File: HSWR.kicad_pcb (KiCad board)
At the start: 4 copper layers, 152 x 139 mm, 158 parts, among them IC1 B1212S-2W, IC2 JW5052C, IC3 JW5052C, IC4 ADUM3054, IC5 ADuM4160, J1 USB_B, J2 IO, J3 B+, J4 B-, J5 U, J6 V, J7 W, J8 SWD, J9 AVR-ISP-6, Q1 IXFK300N20X3, Q2 IXFK300N20X3, Q3 IXFK300N20X3, Q4 IXFK300N20X3, Q5 IXFK300N20X3, Q6 IXFK300N20X3, Q7 Q_NMOS_GSD, U1 ACS781xLRTR-150B, U10 AM26LV32xD, U11 ADuM120N, U12 ADuM120N, U13 PC355, U2 ACS781xLRTR-150B, U3 ACS781xLRTR-150B, U4 STM32F405RGTx, U5 IRS2186, U6 IRS2186, U7 IRS2186, U8 AP1117-50, U9 ATtiny13A-SU, Y1 8MHz

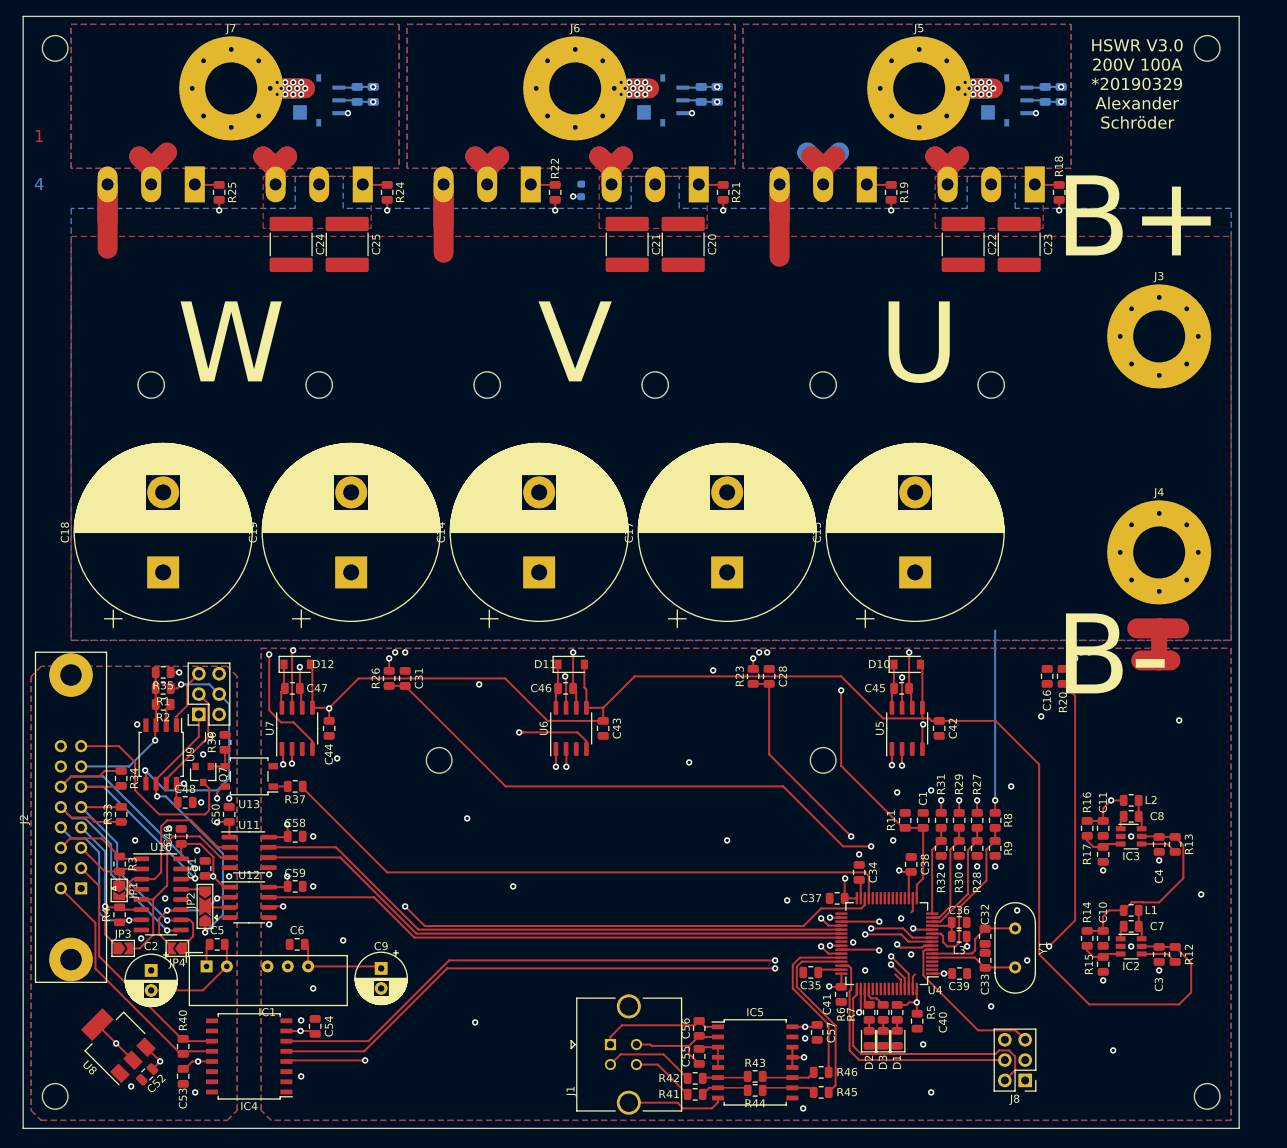
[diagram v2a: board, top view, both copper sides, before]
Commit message: - optimized silk screen - fixed some final missing traces
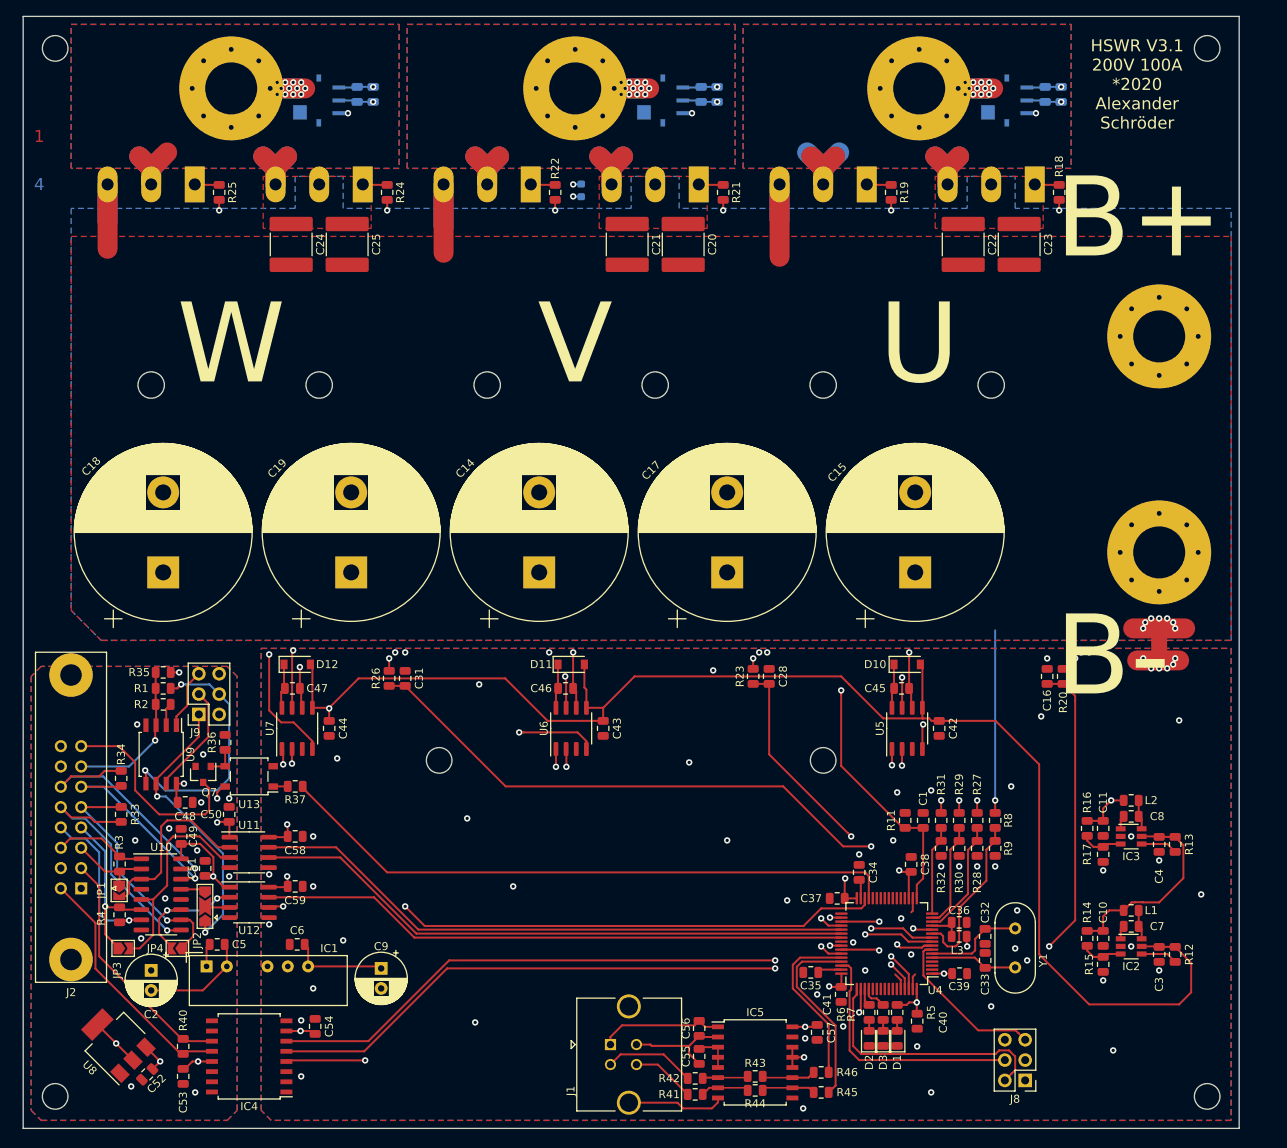
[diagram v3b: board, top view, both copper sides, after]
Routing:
- net +3V3: track 282.3 -> 343.1 mm, vias 18 -> 20
- net /MCU/U_I: track 58.9 -> 60.9 mm
- net GND: track 240.3 -> 241.9 mm, vias 54 -> 65
- net GNDPWR: track 45.4 -> 46.6 mm, vias 0 -> 7
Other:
- board text added: "HSWR V3.1 200V 100A *2020 Alexander Schröder"
- board text removed: "HSWR V3.0 200V 100A *20190329 Alexander Schröder"

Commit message: - fixed ISP connector being mirrored - changed some footprints to get them 3D Models - added a preliminary BOM
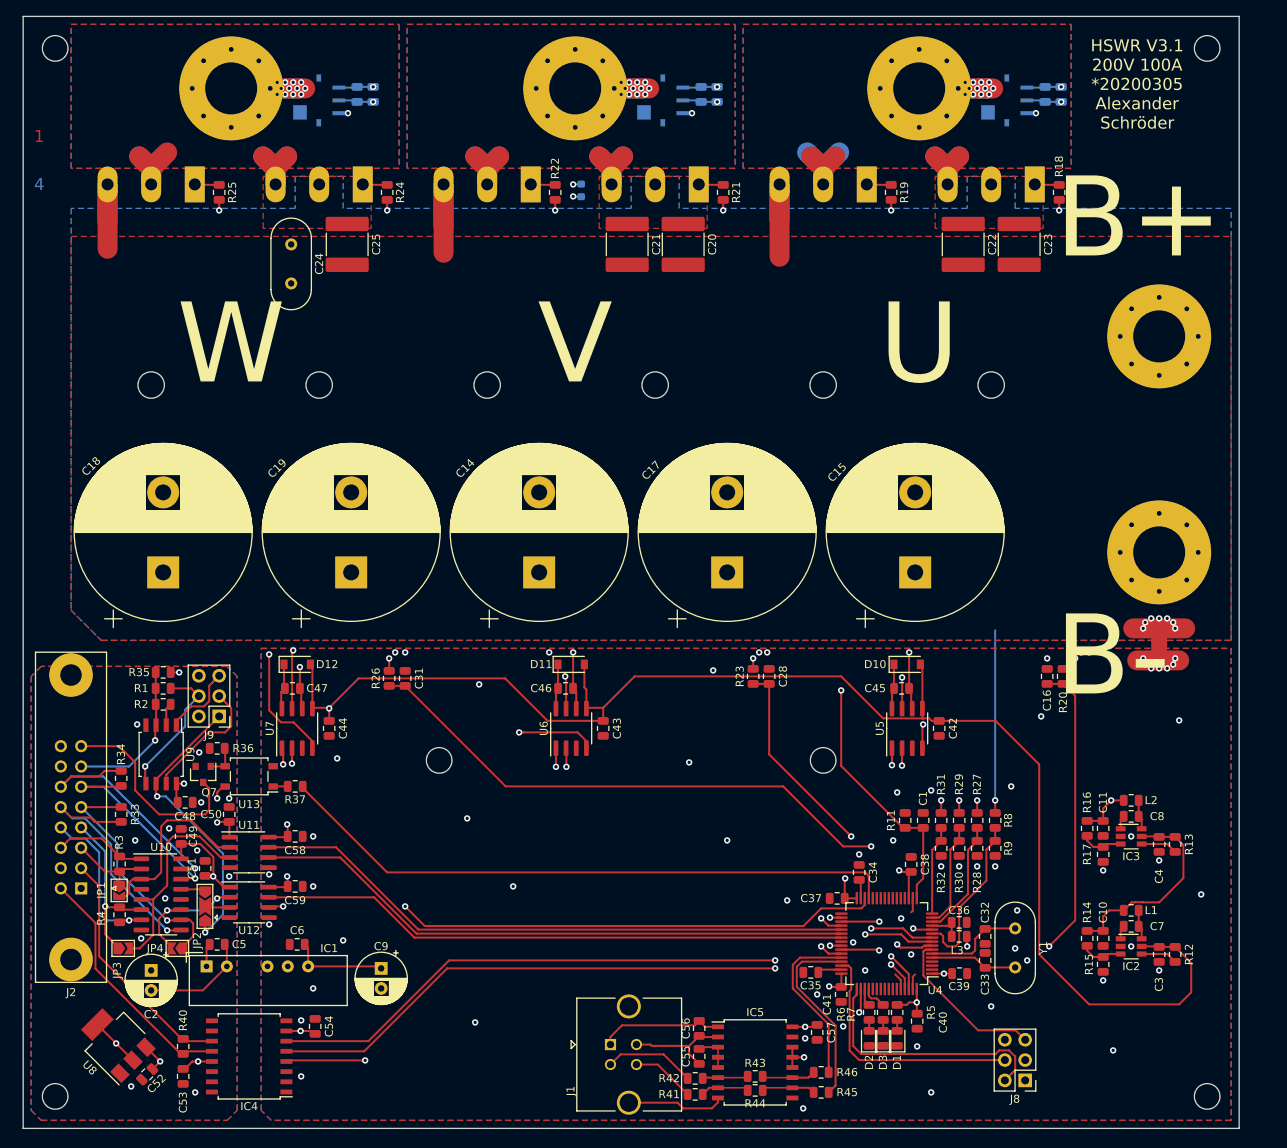
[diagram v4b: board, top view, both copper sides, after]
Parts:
- C24: footprint Capacitor_SMD:C_2220_5650Metric -> Crystal:Crystal_HC49-4H_Vertical
- J9: footprint Connector_PinSocket_2.54mm:PinSocket_2x03_P2.54mm_Vertical -> Connector_PinHeader_2.54mm:PinHeader_2x03_P2.54mm_Vertical
- U5, U6, U7: footprint Package_SO:SO-8_3.9x4.9mm_P1.27mm -> Package_SO:SOIC-8_3.9x4.9mm_P1.27mm
- Y1: footprint Crystal:Crystal_HC49-U_Vertical -> Crystal:Crystal_HC49-4H_Vertical
- moved J9 2.55 mm to (91.5, 111.5)
- moved R36 1.25 mm to (91.2, 115.5), turned to 180 degrees
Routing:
- net Net-(J9-Pad4): track 31.7 -> 17.7 mm, vias 2 -> 1
- net Net-(J9-Pad3): track 13.9 -> 16.1 mm
- net Net-(J9-Pad5): track 7.59 -> 9.33 mm
- net Net-(J9-Pad1): track 35.7 -> 36.5 mm
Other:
- board text added: "HSWR V3.1 200V 100A *20200305 Alexander Schröder"
- board text removed: "HSWR V3.1 200V 100A *2020 Alexander Schröder"

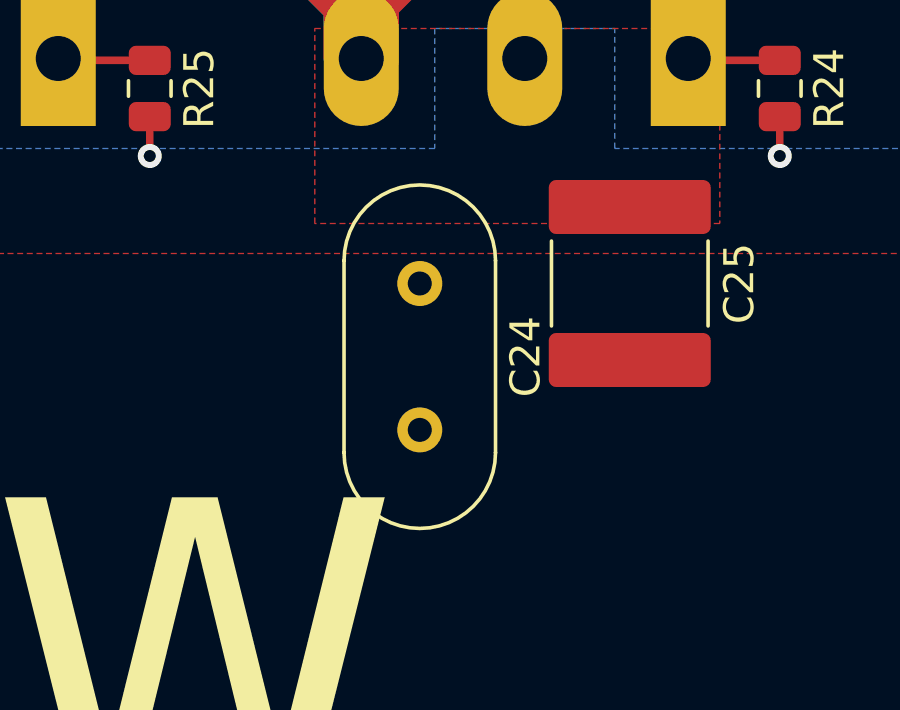
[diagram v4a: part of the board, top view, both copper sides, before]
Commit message: - removed some unused symbols from HSWR.lib - changed U8 (linear reg) to standard symbol - fixed wrong footprint for C24
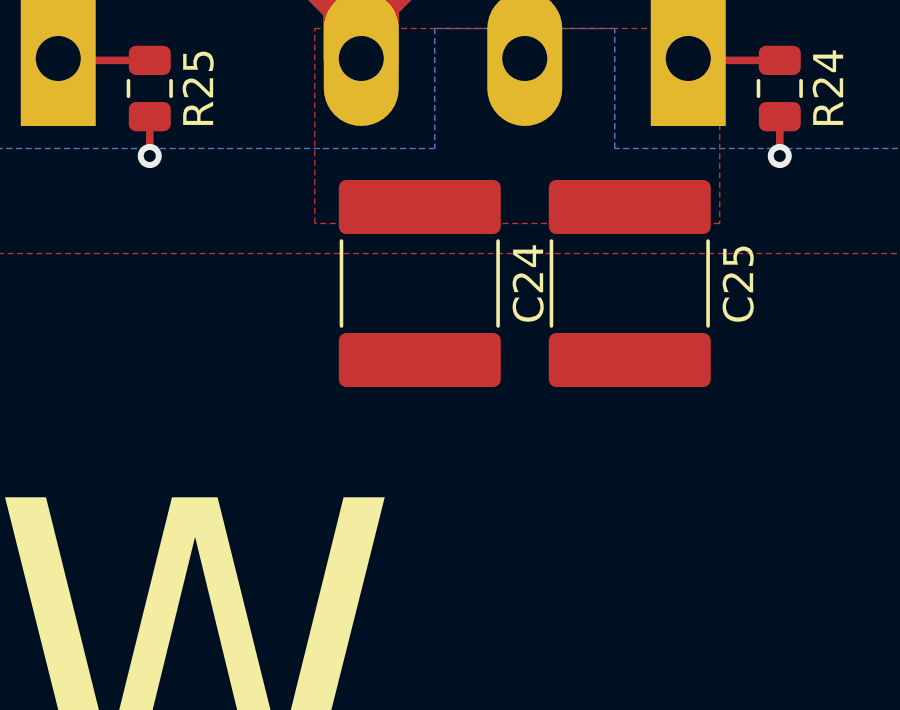
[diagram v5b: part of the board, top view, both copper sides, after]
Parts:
- C24: footprint Crystal:Crystal_HC49-4H_Vertical -> Capacitor_SMD:C_2220_5650Metric
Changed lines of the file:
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@@
     (add_net SWDIO)
   )
+  (module Capacitor_SMD:C_2220_5650Metric (layer F.Cu)
+    (at 100.5 52.5 270)
+    (descr "Capacitor SMD 2220 (5650 Metric), square (rectangular) end terminal, IPC_7351 nominal, (Body size from: http://datasheets.avx.com/AVX-HV_MLCC.pdf), generated with kicad-footprint-generator")
+    (tags capacitor)
+    (attr smd)
+    (fp_text reference C24 (at 0 -3.65 90) (layer F.SilkS)
+      (effects (font (size 1 1) (thickness 0.15)))
+    )
+    (fp_text value "2u2 250V" (at 0 3.65 90) (layer F.Fab)
+      (effects (font (size 1 1) (thickness 0.15)))
+    )
+    (fp_text user %R (at 0 0 90) (layer F.Fab)
+      (effects (font (size 1 1) (thickness 0.15)))
+    )
+    (fp_line (start 3.7 2.95) (end -3.7 2.95) (layer F.CrtYd) (width 0.05))
+    (fp_line (start 3.7 -2.95) (end 3.7 2.95) (layer F.CrtYd) (width 0.05))
+    (fp_line (start -3.7 -2.95) (end 3.7 -2.95) (layer F.CrtYd) (width 0.05))
+    (fp_line (start -3.7 2.95) (end -3.7 -2.95) (layer F.CrtYd) (width 0.05))
+    (fp_line (start -1.415748 2.61) (end 1.415748 2.61) (layer F.SilkS) (width 0.12))
+    (fp_line (start -1.415748 -2.61) (end 1.415748 -2.61) (layer F.SilkS) (width 0.12))
+    (fp_line (start 2.85 2.5) (end -2.85 2.5) (layer F.Fab) (width 0.1))
+    (fp_line (start 2.85 -2.5) (end 2.85 2.5) (layer F.Fab) (width 0.1))
+    (fp_line (start -2.85 -2.5) (end 2.85 -2.5) (layer F.Fab) (width 0.1))
+    (fp_line (start -2.85 2.5) (end -2.85 -2.5) (layer F.Fab) (width 0.1))
+    (pad 2 smd roundrect (at 2.55 0 270) (size 1.8 5.4) (layers F.Cu F.Paste F.Mask) (roundrect_rratio 0.138889)
+      (net 4 GNDPWR))
+    (pad 1 smd roundrect (at -2.55 0 270) (size 1.8 5.4) (layers F.Cu F.Paste F.Mask) (roundrect_rratio 0.138889)
+      (net 13 +BATT))
+    (model ${KISYS3DMOD}/Capacitor_SMD.3dshapes/C_2220_5650Metric.wrl
+      (at (xyz 0 0 0))
+      (scale (xyz 1 1 1))
+      (rotate (xyz 0 0 0))
+    )
+  )
+  (module Package_TO_SOT_SMD:SOT-223-3_TabPin2 (layer F.Cu)
+    (at 78.5 152.25 135)
+    (descr "module CMS SOT223 4 pins")
+    (tags "CMS SOT")
+    (attr smd)
+    (fp_text reference U8 (at 0 -4.5 135) (layer F.SilkS)
+      (effects (font (size 1 1) (thickness 0.15)))
+    )
+    (fp_text value AP1117-50 (at 0 4.5 135) (layer F.Fab)
+      (effects (font (size 1 1) (thickness 0.15)))
+    )
+    (fp_line (start 1.85 -3.35) (end 1.85 3.35) (layer F.Fab) (width 0.1))
+    (fp_line (start -1.85 3.35) (end 1.85 3.35) (layer F.Fab) (width 0.1))
+    (fp_line (start -4.1 -3.41) (end 1.91 -3.41) (layer F.SilkS) (width 0.12))
+    (fp_line (start -0.85 -3.35) (end 1.85 -3.35) (layer F.Fab) (width 0.1))
+    (fp_line (start -1.85 3.41) (end 1.91 3.41) (layer F.SilkS) (width 0.12))
+    (fp_line (start -1.85 -2.35) (end -1.85 3.35) (layer F.Fab) (width 0.1))
+    (fp_line (start -1.85 -2.35) (end -0.85 -3.35) (layer F.Fab) (width 0.1))
+    (fp_line (start -4.4 -3.6) (end -4.4 3.6) (layer F.CrtYd) (width 0.05))
+    (fp_line (start -4.4 3.6) (end 4.4 3.6) (layer F.CrtYd) (width 0.05))
+    (fp_line (start 4.4 3.6) (end 4.4 -3.6) (layer F.CrtYd) (width 0.05))
+    (fp_line (start 4.4 -3.6) (end -4.4 -3.6) (layer F.CrtYd) (width 0.05))
+    (fp_line (start 1.91 -3.41) (end 1.91 -2.15) (layer F.SilkS) (width 0.12))
+    (fp_line (start 1.91 3.41) (end 1.91 2.15) (layer F.SilkS) (width 0.12))
+    (fp_text user %R (at 0 0 45) (layer F.Fab)
+      (effects (font (size 0.8 0.8) (thickness 0.12)))
+    )
+    (pad 1 smd rect (at -3.15 -2.3 135) (size 2 1.5) (layers F.Cu F.Paste F.Mask)
+      (net 1 Earth))
+    (pad 3 smd rect (at -3.15 2.3 135) (size 2 1.5) (layers F.Cu F.Paste F.Mask)
+      (net 56 +12VA))
+    (pad 2 smd rect (at -3.15 0 135) (size 2 1.5) (layers F.Cu F.Paste F.Mask)
+      (net 84 +5VA))
+    (pad 2 smd rect (at 3.15 0 135) (size 2 3.8) (layers F.Cu F.Paste F.Mask)
+      (net 84 +5VA))
+    (model ${KISYS3DMOD}/Package_TO_SOT_SMD.3dshapes/SOT-223.wrl
+      (at (xyz 0 0 0))
+      (scale (xyz 1 1 1))
+      (rotate (xyz 0 0 0))
+    )
+  )
   (module Connector_PinHeader_2.54mm:PinHeader_2x03_P2.54mm_Vertical (layer F.Cu)
     (at 91.5 111.5 180)
@@
     )
   )
-  (module Crystal:Crystal_HC49-4H_Vertical (layer F.Cu)
-    (at 100.5 52.5 270)
-    (descr "Crystal THT HC-49-4H http://5hertz.com/pdfs/04404_D.pdf")
-    (tags "THT crystalHC-49-4H")
-    (fp_text reference C24 (at 2.44 -3.525 90) (layer F.SilkS)
-      (effects (font (size 1 1) (thickness 0.15)))
-    )
-    (fp_text value "2u2 250V" (at 2.44 3.525 90) (layer F.Fab)
-      (effects (font (size 1 1) (thickness 0.15)))
-    )
-    (fp_arc (start 5.64 0) (end 5.64 -2.525) (angle 180) (layer F.SilkS) (width 0.12))
-    (fp_arc (start -0.76 0) (end -0.76 -2.525) (angle -180) (layer F.SilkS) (width 0.12))
-    (fp_arc (start 5.44 0) (end 5.44 -2) (angle 180) (layer F.Fab) (width 0.1))
-    (fp_arc (start -0.56 0) (end -0.56 -2) (angle -180) (layer F.Fab) (width 0.1))
-    (fp_arc (start 5.64 0) (end 5.64 -2.325) (angle 180) (layer F.Fab) (width 0.1))
-    (fp_arc (start -0.76 0) (end -0.76 -2.325) (angle -180) (layer F.Fab) (width 0.1))
-    (fp_line (start 8.5 -2.8) (end -3.6 -2.8) (layer F.CrtYd) (width 0.05))
-    (fp_line (start 8.5 2.8) (end 8.5 -2.8) (layer F.CrtYd) (width 0.05))
-    (fp_line (start -3.6 2.8) (end 8.5 2.8) (layer F.CrtYd) (width 0.05))
-    (fp_line (start -3.6 -2.8) (end -3.6 2.8) (layer F.CrtYd) (width 0.05))
-    (fp_line (start -0.76 2.525) (end 5.64 2.525) (layer F.SilkS) (width 0.12))
-    (fp_line (start -0.76 -2.525) (end 5.64 -2.525) (layer F.SilkS) (width 0.12))
-    (fp_line (start -0.56 2) (end 5.44 2) (layer F.Fab) (width 0.1))
-    (fp_line (start -0.56 -2) (end 5.44 -2) (layer F.Fab) (width 0.1))
-    (fp_line (start -0.76 2.325) (end 5.64 2.325) (layer F.Fab) (width 0.1))
-    (fp_line (start -0.76 -2.325) (end 5.64 -2.325) (layer F.Fab) (width 0.1))
-    (fp_text user %R (at 2.44 0 90) (layer F.Fab)
-      (effects (font (size 1 1) (thickness 0.15)))
-    )
-    (pad 2 thru_hole circle (at 4.88 0 270) (size 1.5 1.5) (drill 0.8) (layers *.Cu *.Mask)
-      (net 4 GNDPWR))
-    (pad 1 thru_hole circle (at 0 0 270) (size 1.5 1.5) (drill 0.8) (layers *.Cu *.Mask)
-      (net 13 +BATT))
-    (model ${KISYS3DMOD}/Crystal.3dshapes/Crystal_HC49-4H_Vertical.wrl
-      (at (xyz 0 0 0))
-      (scale (xyz 1 1 1))
-      (rotate (xyz 0 0 0))
-    )
-  )
   (module Package_SO:SOIC-8_3.9x4.9mm_P1.27mm (layer F.Cu)
     (at 101.25 113 90)
@@
       (at (xyz 0 0 0))
       (scale (xyz 1 1 1))
-      (rotate (xyz 0 0 0))
-    )
-  )
-  (module Package_TO_SOT_SMD:SOT-223-3_TabPin2 (layer F.Cu)
-    (at 78.5 152.25 135)
-    (descr "module CMS SOT223 4 pins")
-    (tags "CMS SOT")
-    (attr smd)
-    (fp_text reference U8 (at 0 -4.5 135) (layer F.SilkS)
-      (effects (font (size 1 1) (thickness 0.15)))
-    )
-    (fp_text value AP1117-50 (at 0 4.5 135) (layer F.Fab)
-      (effects (font (size 1 1) (thickness 0.15)))
-    )
-    (fp_text user %R (at 0 0 225) (layer F.Fab)
-      (effects (font (size 0.8 0.8) (thickness 0.12)))
-    )
-    (fp_line (start 1.91 3.41) (end 1.91 2.15) (layer F.SilkS) (width 0.12))
-    (fp_line (start 1.91 -3.41) (end 1.91 -2.15) (layer F.SilkS) (width 0.12))
-    (fp_line (start 4.4 -3.6) (end -4.4 -3.6) (layer F.CrtYd) (width 0.05))
-    (fp_line (start 4.4 3.6) (end 4.4 -3.6) (layer F.CrtYd) (width 0.05))
-    (fp_line (start -4.4 3.6) (end 4.4 3.6) (layer F.CrtYd) (width 0.05))
-    (fp_line (start -4.4 -3.6) (end -4.4 3.6) (layer F.CrtYd) (width 0.05))
-    (fp_line (start -1.85 -2.35) (end -0.85 -3.35) (layer F.Fab) (width 0.1))
-    (fp_line (start -1.85 -2.35) (end -1.85 3.35) (layer F.Fab) (width 0.1))
-    (fp_line (start -1.85 3.41) (end 1.91 3.41) (layer F.SilkS) (width 0.12))
-    (fp_line (start -0.85 -3.35) (end 1.85 -3.35) (layer F.Fab) (width 0.1))
-    (fp_line (start -4.1 -3.41) (end 1.91 -3.41) (layer F.SilkS) (width 0.12))
-    (fp_line (start -1.85 3.35) (end 1.85 3.35) (layer F.Fab) (width 0.1))
-    (fp_line (start 1.85 -3.35) (end 1.85 3.35) (layer F.Fab) (width 0.1))
-    (pad 2 smd rect (at 3.149999 0 135) (size 2 3.8) (layers F.Cu F.Paste F.Mask)
-      (net 84 +5VA))
-    (pad 2 smd rect (at -3.149999 0 135) (size 2 1.5) (layers F.Cu F.Paste F.Mask)
-      (net 84 +5VA))
-    (pad 3 smd rect (at -3.15 2.3 135) (size 2 1.5) (layers F.Cu F.Paste F.Mask)
-      (net 56 +12VA))
-    (pad 1 smd rect (at -3.15 -2.3 135) (size 2 1.5) (layers F.Cu F.Paste F.Mask)
-      (net 1 Earth))
-    (model ${KISYS3DMOD}/Package_TO_SOT_SMD.3dshapes/SOT-223.wrl
-      (at (xyz 0 0 0))
-      (scale (xyz 1 1 1))
